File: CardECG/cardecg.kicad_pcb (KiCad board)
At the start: 2 copper layers, 39 parts, among them P1 CONN_7, P2 BATTERY, Q1 FET_P2, Q2 FET_P2, U1 OPAMP1, U2 TPS717, U3 ADuC7061, U4 SSD1306

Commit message: New PCB
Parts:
- removed D1: ZENER 3.6V, Diodes_SMD:SOD-323
- removed JP1, JP2: JUMPER, Capacitors_SMD:C_0402
- removed SP1: SPEAKER, Pin_Headers:Pin_Header_Straight_1x02
- added CN1: 2TAP, mod:2TAP, F.Cu at (81.0, 73.7)
- added D6: D, Diodes_SMD:SOD-323, F.Cu at (55.9, 52.9)
- added P3: FORCE ON, Pin_Headers:Pin_Header_Straight_1x02, F.Cu at (84.3, 59.4)
- added Q3: BSS84P, Housings_SOT-23_SOT-143_TSOT-6:SOT-23, F.Cu at (52.1, 60.9)
- added Q4: NTR1P02T1, Housings_SOT-23_SOT-143_TSOT-6:SOT-23, F.Cu at (55.4, 57.9)
- added Q5: NMOS_GSD, Housings_SOT-23_SOT-143_TSOT-6:SOT-23, F.Cu at (52.1, 54.6)
- added Q6: NMOS_GSD, Housings_SOT-23_SOT-143_TSOT-6:SOT-23, F.Cu at (81.1, 53.8)
- added Q7: NTR1P02T1, Housings_SOT-23_SOT-143_TSOT-6:SOT-23, F.Cu at (84.6, 55.6)
- added R10: 100k, Resistors_SMD:R_0603, F.Cu at (84.4, 53.0)
- added R11: 100k, Resistors_SMD:R_0603, F.Cu at (81.2, 56.5)
- added R12: 47k, Resistors_SMD:R_0603, F.Cu at (57.7, 72.4)
- added R13: 47k, Resistors_SMD:R_0603, F.Cu at (59.9, 72.1)
- added R14: 47k, Resistors_SMD:R_0603, F.Cu at (63.6, 70.0)
- added R15: 47k, Resistors_SMD:R_0603, F.Cu at (62.6, 71.7)
- added R7: 20M, Resistors_SMD:R_0603, F.Cu at (55.3, 61.0)
- added R8: 100k, Resistors_SMD:R_0603, F.Cu at (52.9, 57.7)
- added R9: 100k, Resistors_SMD:R_0603, F.Cu at (51.2, 57.7)
- added U5: creditcard, mod:creditcard, F.Cu at (0.00, 0.00)
- added U6: DNP, Capacitors_SMD:C_0603, F.Cu at (85.9, 73.0)
- added U7: DNP, Capacitors_SMD:C_0603, F.Cu at (51.4, 73.0)
- D2, D3, D4, D5: value DIODE -> D
- P1: value CONN_7 -> PROG
- Q1: value FET_P2 -> BSS84P; footprint TO_SOT_Packages_SMD:SOT-23 -> Housings_SOT-23_SOT-143_TSOT-6:SOT-23
- Q2: value FET_P2 -> NTR1P02T1; footprint TO_SOT_Packages_SMD:SOT-23 -> Housings_SOT-23_SOT-143_TSOT-6:SOT-23
- R1, R2, R3, R4, R5, R6: footprint Capacitors_SMD:C_0603 -> Resistors_SMD:R_0603
- U1: value OPAMP1 -> LMV341
- moved R5 1.65 mm to (65.3, 72.4)
- moved C11 0.67 mm to (68.8, 62.8)
- moved D3 0.25 mm to (84.4, 70.2)
- moved D4 0.16 mm to (52.5, 66.4)
- turned C1 to 270 degrees
- turned R2 to 270 degrees
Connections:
- C10 pad 1: /vbat2 -> VCC
- D2 pad 1: Net-(C2-Pad1) -> +BATT
- D2 pad 2: +BATT -> Net-(C2-Pad1)
- D3 pad 1: GND -> Net-(C2-Pad1)
- D3 pad 2: Net-(C2-Pad1) -> GND
- D4 pad 1: Net-(D4-Pad1) -> +BATT
- D4 pad 2: +BATT -> Net-(D4-Pad2)
- D5 pad 1: GND -> Net-(D4-Pad2)
- D5 pad 2: Net-(D4-Pad1) -> GND
- P1 pad 1: GND -> ~FORCE_ON
- P1 pad 2: /reset -> GND
- P1 pad 3: /tms -> +BATT
- P1 pad 4: /ntrst -> ~RESET
- P1 pad 5: /tdo -> ~PROG
- P1 pad 6: /tdi -> RX
- P1 pad 7: /tck -> TX
- Q1 pad 1: Net-(D4-Pad1) -> Net-(D4-Pad2)
- Q1 pad 3: Net-(JP2-Pad2) -> Net-(D6-Pad1)
- R1 pad 1: Net-(JP2-Pad2) -> Net-(D6-Pad1)
- R2 pad 2: Net-(D4-Pad1) -> Net-(D4-Pad2)
- R5 pad 1: /reset -> ~RESET
- R6 pad 1: Net-(D4-Pad1) -> Net-(D4-Pad2)
- R6 pad 2: +BATT -> Net-(Q3-Pad3)
- U1 pad 1: Net-(R3-Pad2) -> Net-(C1-Pad1)
- U1 pad 3: Net-(C1-Pad1) -> Net-(R3-Pad2)
- U1 pad 5: Net-(JP2-Pad2) -> VCC
- U2 pad 3: Net-(JP2-Pad2) -> VCC
- U3 pad 1: /reset -> ~RESET
- U3 pad 10: Net-(U3-Pad10) -> (no net)
- U3 pad 11: Net-(U3-Pad11) -> (no net)
- U3 pad 12: Net-(U3-Pad12) -> GND
- U3 pad 17: Net-(U3-Pad17) -> GND
- U3 pad 18: Net-(U3-Pad18) -> GND
- U3 pad 2: /tms -> Net-(R12-Pad2)
- U3 pad 23: Net-(U3-Pad23) -> (no net)
- U3 pad 24: Net-(U3-Pad24) -> (no net)
- U3 pad 25: Net-(SP1-Pad1) -> PULLUP_OFF
- U3 pad 26: Net-(SP1-Pad2) -> POWER_ON
- U3 pad 29: /ntrst -> ~PROG
- U3 pad 3: Net-(U3-Pad3) -> RX
- U3 pad 30: /tdo -> (no net)
- U3 pad 31: /tdi -> Net-(R14-Pad1)
- U3 pad 32: /tck -> Net-(R15-Pad1)
- U3 pad 33: GND -> Net-(CN1-Pad1)
- U3 pad 4: Net-(U3-Pad4) -> TX
- U3 pad 6: Net-(U3-Pad6) -> GND
- U3 pad 7: Net-(U3-Pad7) -> GND
- U3 pad 8: Net-(U3-Pad8) -> GND
- U3 pad 9: Net-(U3-Pad9) -> GND
- U4 pad 6: /vbat2 -> VCC
- U4 pad 7: Net-(U4-Pad7) -> (no net)
- left1 pad 1: Net-(D4-Pad1) -> Net-(D4-Pad2)
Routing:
- net VCC: track 0.00 -> 75.3 mm, vias 0 -> 4
- net ~FORCE_ON: track 0.00 -> 64.1 mm, vias 0 -> 1
- net GND: track 320.7 -> 368.4 mm, vias 30 -> 35
- net Net-(D6-Pad1): track 0.00 -> 42.4 mm, vias 0 -> 3
- net Net-(JP2-Pad2): track 39.6 -> 0.00 mm, vias 2 -> 0
- net PULLUP_OFF: track 0.00 -> 34.9 mm, vias 0 -> 2
- net Net-(D4-Pad2): track 0.00 -> 34.6 mm
- net /vbat2: track 32.2 -> 0.00 mm, vias 2 -> 0
- net +BATT: track 59.6 -> 89.1 mm, vias 4 -> 5
- net Net-(D4-Pad1): track 28.6 -> 0.00 mm
- net ~PROG: track 0.00 -> 25.4 mm, vias 0 -> 1
- net POWER_ON: track 0.00 -> 22.7 mm, vias 0 -> 2
- net Net-(SP1-Pad2): track 20.4 -> 0.00 mm, vias 1 -> 0
- net /tdi: track 19.4 -> 0.00 mm, vias 1 -> 0
- net Net-(SP1-Pad1): track 19.0 -> 0.00 mm, vias 1 -> 0
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
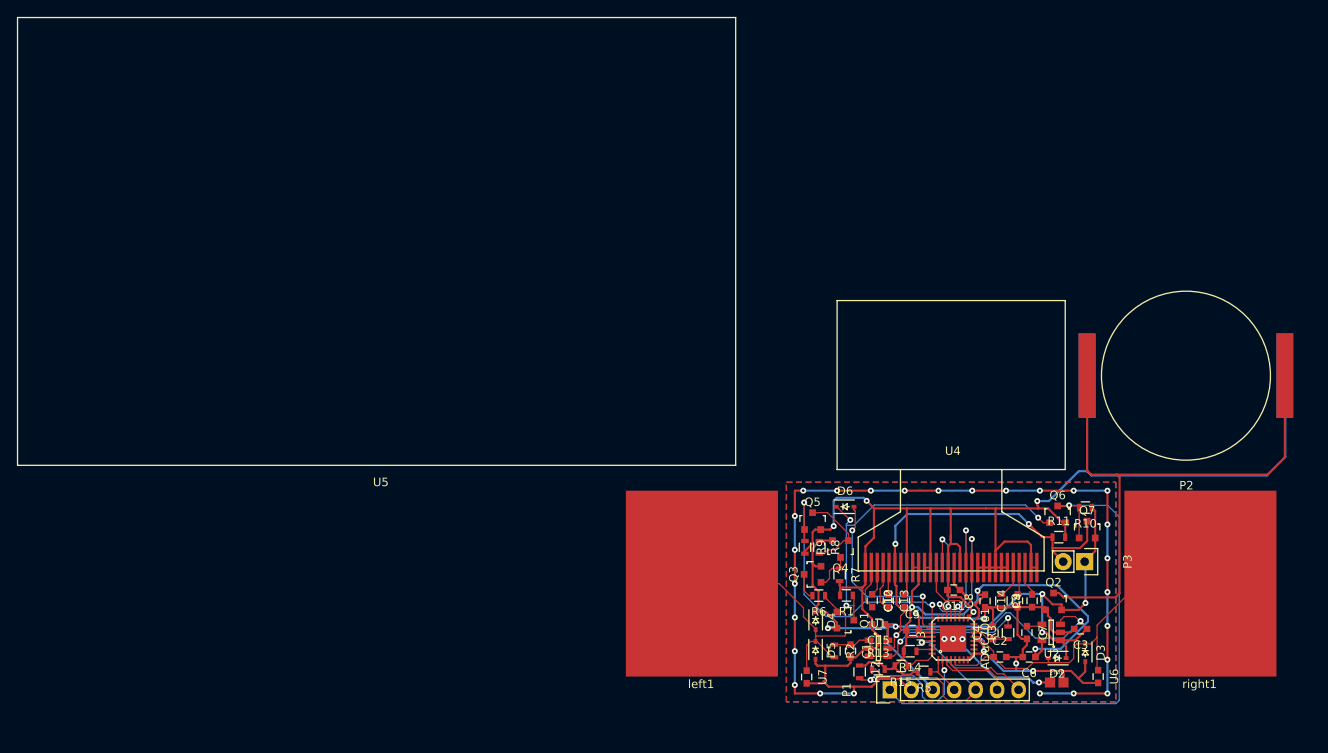
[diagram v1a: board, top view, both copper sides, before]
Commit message: Added filter cap for the first switch transistor
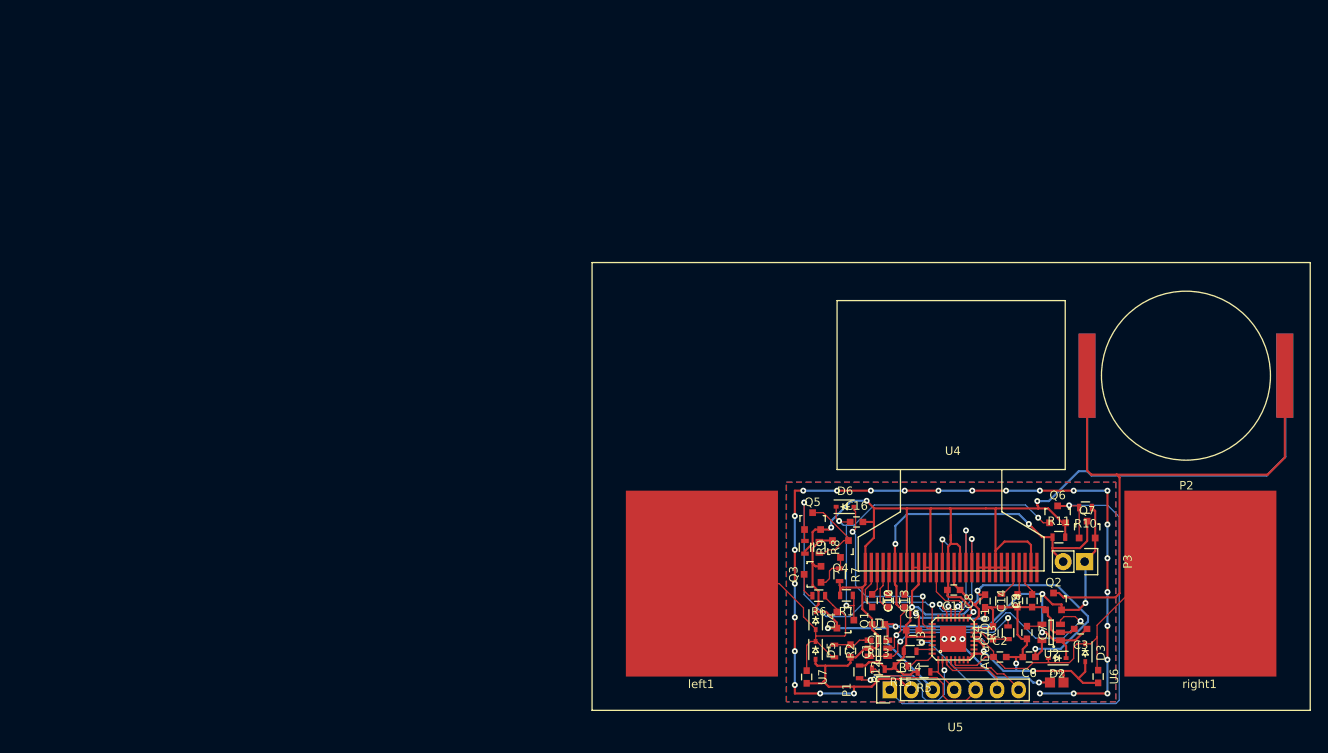
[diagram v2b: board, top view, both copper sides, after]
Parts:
- added C16: 100nF, Capacitors_SMD:C_0603, F.Cu at (57.3, 54.7)
- moved U5 73.9 mm to (68.0, 29.0)
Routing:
- net Net-(C16-Pad1): track 42.4 -> 43.8 mm
- net GND: track 368.4 -> 367.8 mm
